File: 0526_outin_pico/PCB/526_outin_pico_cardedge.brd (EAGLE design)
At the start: 53 x 28.9 mm, 5 parts

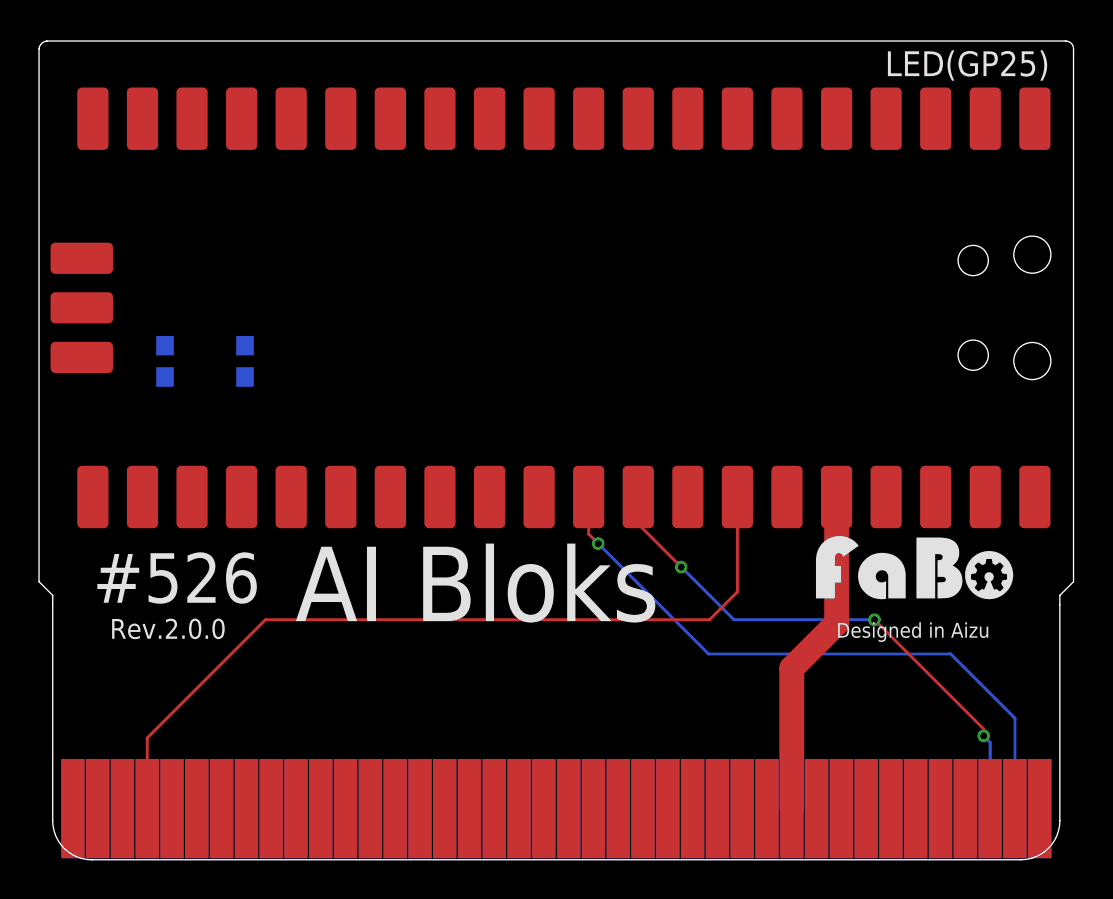
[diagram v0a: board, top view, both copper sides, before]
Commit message: #527 AI BLOCKS追加　Rev1.0.0 alpha
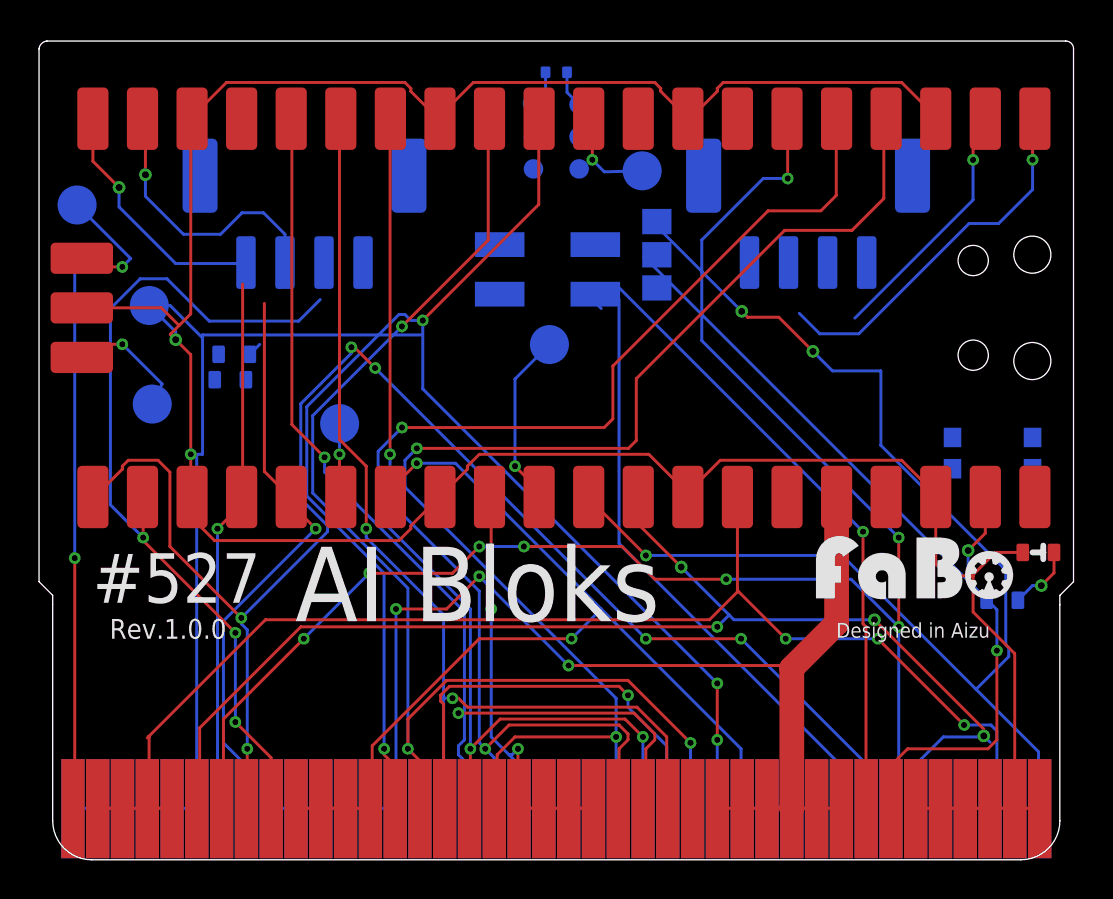
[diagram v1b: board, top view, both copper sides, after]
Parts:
- added C1: 0.1uF, FaBo-Capacitor:0402
- added CN1, CN2: (no value), FaBo-Connetor:SM04B-PASS
- added GP7, TP1, TP10, TP2, TP3, TP4: TPSQTP20R, testpad:TP20R
- added JMP1: 0R-JUMPA, jump-0r-smd:A0R-JMP
- added LED1: (no value), FaBo-LED:0603
- added R1: 470, FaBo-Resistors:0603
- added R2, R3: (no value), FaBo-Resistors:0603
- added SJ1, SJ2: (no value), jumper:SJW
- added U$1: SPM0405H, FaBo-Sensor:SPM4050
- moved S2 40.6 mm to (48.9, 20.8)
- moved LOGO1 25.1 mm to (13.0, 8.64)
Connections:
- net D5 renamed D5_PWM
- removed net PWM14: U1.19
- removed net PWM15: U1.20
- removed net PWM16: U1.21
- removed net PWM17: U1.22
- removed net SCL: U1.12
- removed net SDA: U1.11
- new net D6_PWM: U1.9
- new net D8: U$2.P$14, U$2.P$54, U1.11
- new net D9_LEDS: U$2.P$15, U$2.P$55, U1.12
- new net GP14: CN2.2, U1.19
- new net GP15: CN2.1, U1.20
- new net GP16: U$2.P$16, U$2.P$56
- new net GP16_PWM_UART0_TX: U$2.P$48, U$2.P$8, U1.21
- new net GP17_PWM_UART0_RX: U$2.P$49, U$2.P$9, U1.22
- new net I2C1_SCL: R2.1, U$2.P$33, U$2.P$73, U1.25
- new net I2C1_SDA: R3.1, U$2.P$34, U$2.P$74, U1.24
- new net N$1: R1.1, U1.39
- new net N$2: LED1.ANODE, R1.2
- new net N$3: GP7.TP, U1.10
- new net N$4: TP10.TP, U1.26
- new net N$5: JMP1.2, U$1.2:LEFT/RIGHT
- new net N$6: SJ1.1, U$1.4:CLOCK
- new net N$7: SJ2.1, U$1.5:DATA
- new net PDM_CLK: SJ1.2, U$2.P$10, U$2.P$11, U$2.P$12, U$2.P$13, U$2.P$50, U$2.P$51, U$2.P$52, U$2.P$53, U1.27
- new net PDM_DIN: SJ2.2, U$2.P$19, U$2.P$20, U$2.P$21, U$2.P$22, U$2.P$59, U$2.P$60, U$2.P$61, U$2.P$62, U1.29
- new net SPI1_CSN: U1.17
- new net SPI1_RX: U$2.P$24, U$2.P$64, U1.16
- new net SPI1_SCK: U$2.P$23, U$2.P$63, U1.14
- new net SPI1_TX: U$2.P$25, U$2.P$65, U1.15
- net 3V3: now also C1.2, CN1.3, CN2.3, JMP1.1, R2.2, R3.2, U$1.6:VDD
- net A0: now also U$2.P$1, U$2.P$41; no longer U$2.P$2, U$2.P$42
- net A1: now also U$2.P$46, U$2.P$6; no longer U$2.P$3, U$2.P$43
- net A2: now also U$2.P$2, U$2.P$3, U$2.P$42, U$2.P$43, U$2.P$45, U$2.P$5
- net D2: now also U$2.P$18, U$2.P$58
- net D3: now also U$2.P$17, U$2.P$57
- net D4: now also U$2.P$47, U$2.P$7
- net GND: now also C1.1, CN1.4, CN2.4, JMP1.3, LED1.CATHODE, TP3.TP, U$1.1:GND, U$1.3:GND
- net RESET: now also TP4.TP
- net RX: now also CN1.1
- net SWCLK: now also TP1.TP
- net SWDIO: now also TP2.TP
- net TX: now also CN1.2
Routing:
- net GND: track 0.00 -> 194.1 mm, vias 0 -> 2
- net D4: track 0.00 -> 86.9 mm, vias 0 -> 8
- net GP16_PWM_UART0_TX: track 0.00 -> 78.8 mm, vias 0 -> 6
- net GP17_PWM_UART0_RX: track 0.00 -> 74.7 mm, vias 0 -> 3
- net D8: track 0.00 -> 74.6 mm, vias 0 -> 4
- net I2C1_SDA: track 0.00 -> 68.7 mm, vias 0 -> 2
- net D3: track 0.00 -> 68.2 mm, vias 0 -> 3
- net D2: track 0.00 -> 67.9 mm, vias 0 -> 2
- net D9_LEDS: track 0.00 -> 63.0 mm, vias 0 -> 3
- net I2C1_SCL: track 0.00 -> 61.6 mm, vias 0 -> 2
- net A0: track 32.9 -> 92.8 mm, vias 1 -> 4
- net SPI1_RX: track 0.00 -> 54.4 mm, vias 0 -> 2
- net PDM_CLK: track 0.00 -> 53.7 mm, vias 0 -> 2
- net SPI1_TX: track 0.00 -> 53.6 mm, vias 0 -> 2
- net SPI1_SCK: track 0.00 -> 49.6 mm, vias 0 -> 2
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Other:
- board text added: "#527"
- board text added: "3V"
- board text added: "A0"
- board text added: "A2"
- board text added: "GND"
- board text added: "MIC"
- board text added: "Rev.1.0.0"
- board text removed: "#526"
- board text removed: "LED(GP25)"
- board text removed: "Rev.2.0.0"
